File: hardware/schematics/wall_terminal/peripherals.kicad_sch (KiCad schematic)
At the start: 4 parts, among them U11 MAX487E

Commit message: !refactor
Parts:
- removed R31: 10k, symbol Device:R
- removed R32: 18k, symbol Device:R
- removed R33: 120, symbol Device:R
- removed U11: MAX487E, Package_DIP:DIP-8_W7.62mm_Socket, symbol Interface_UART:MAX487E
- added R10: 1k, Resistor_THT:R_Axial_DIN0207_L6.3mm_D2.5mm_P2.54mm_Vertical, symbol Device:R
- added R11: 120, Resistor_THT:R_Axial_DIN0207_L6.3mm_D2.5mm_P7.62mm_Horizontal, symbol Device:R
- added U2: MAX487E, Package_DIP:DIP-8_W7.62mm_Socket, symbol Interface_UART:MAX487E
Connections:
- net 5V: now also U2.8 (VCC)
- net A: now also R11.1, U2.6 (A)
- net B: now also R11.2, U2.7 (B)
- net GND: now also U2.5 (GND)
- new net: R10.1, U2.1 (RO)
- new net DE/~{RE}: U2.2 (~{RE}), U2.3 (DE)
- new net RX/TX: R10.2, U2.4 (DI)
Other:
- title: Domoticata main control unit -> Domoticata wall terminal

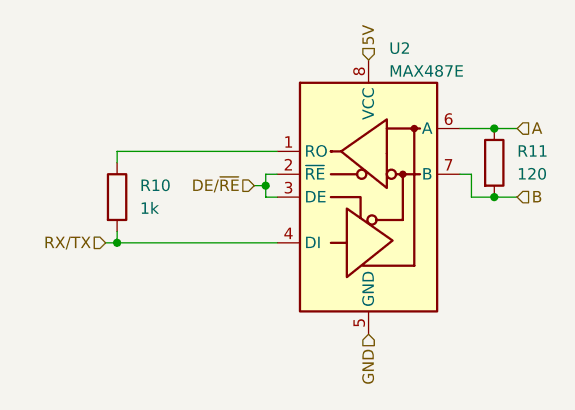
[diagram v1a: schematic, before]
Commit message: fix: added optional resistors on PWM outputs.
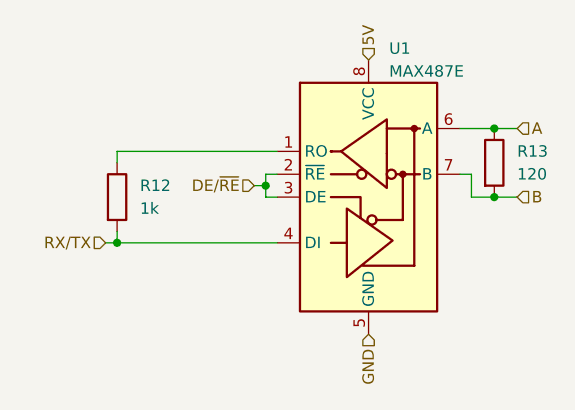
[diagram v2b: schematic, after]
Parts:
- renumbered R10 to R12, R11 to R13, U2 to U1
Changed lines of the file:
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@@
 		(dnp no)
 		(fields_autoplaced yes)
-		(property "Reference" "R10"
+		(property "Reference" "R12"
 			(at 120.65 87.6299 0)
 			(effects
@@
 			(project "wall_terminal"
 				(path "/5c441dea-07fa-47c6-a7dc-b1c524c62a23/0256ce06-ee3b-4689-a32f-e794e2021f9c"
-					(reference "R10")
+					(reference "R12")
 					(unit 1)
 				)
@@
 		(on_board yes)
 		(dnp no)
-		(property "Reference" "U2"
+		(property "Reference" "U1"
 			(at 148.336 72.39 0)
 			(effects
@@
 			(project "wall_terminal"
 				(path "/5c441dea-07fa-47c6-a7dc-b1c524c62a23/0256ce06-ee3b-4689-a32f-e794e2021f9c"
-					(reference "U2")
+					(reference "U1")
 					(unit 1)
 				)
@@
 		(dnp no)
 		(fields_autoplaced yes)
-		(property "Reference" "R11"
+		(property "Reference" "R13"
 			(at 162.56 83.8199 0)
 			(effects
@@
 			(project ""
 				(path "/5c441dea-07fa-47c6-a7dc-b1c524c62a23/0256ce06-ee3b-4689-a32f-e794e2021f9c"
-					(reference "R11")
+					(reference "R13")
 					(unit 1)
 				)
